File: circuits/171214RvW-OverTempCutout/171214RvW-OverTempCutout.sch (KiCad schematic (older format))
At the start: 6 parts

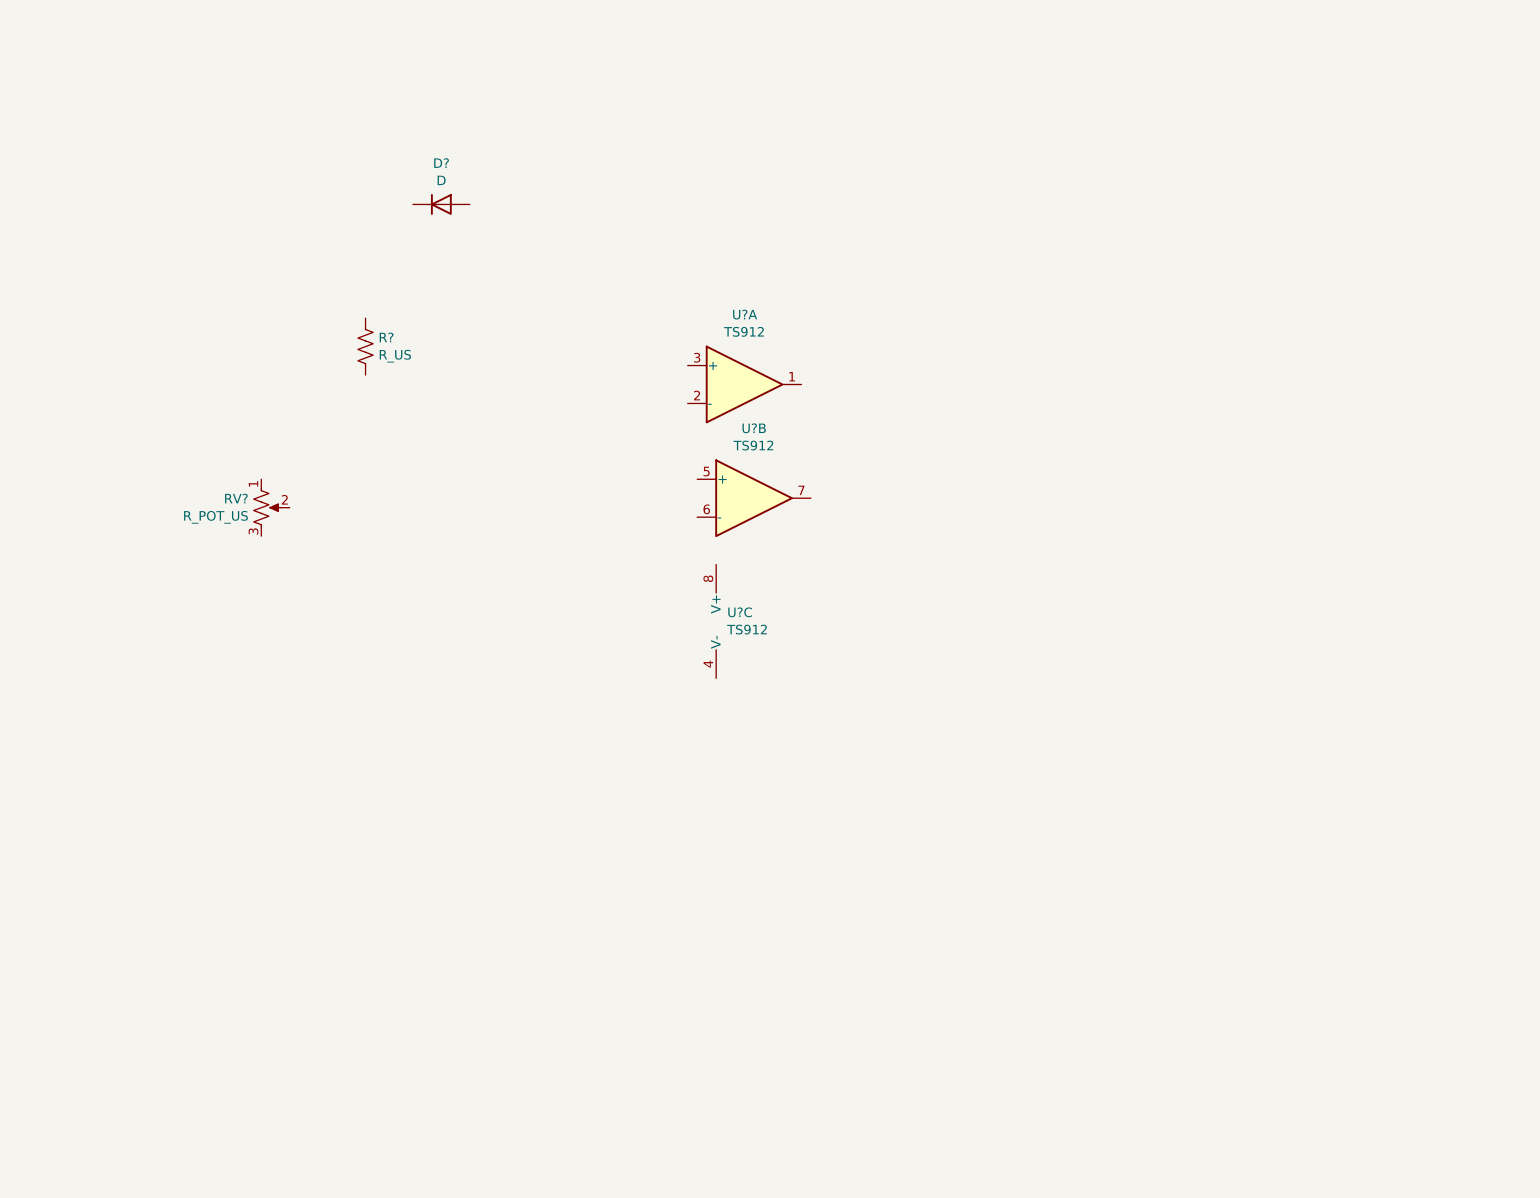
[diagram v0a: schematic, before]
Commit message: Overtemp Cutout done
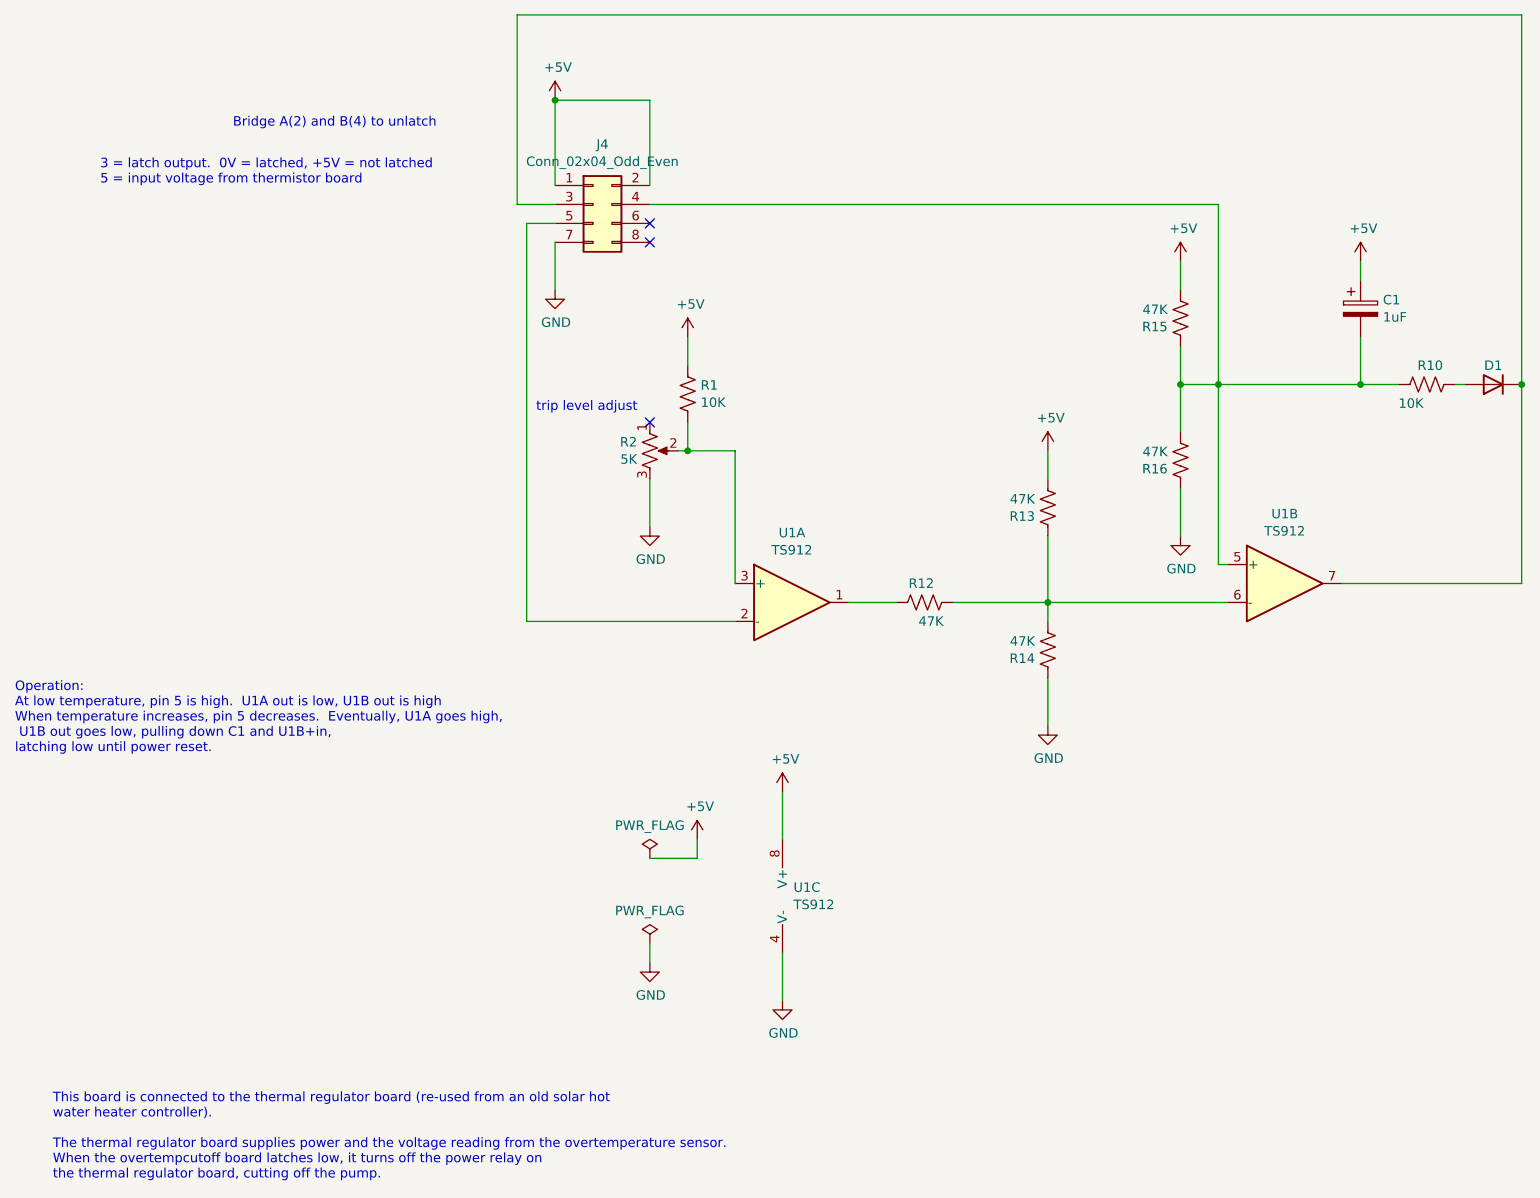
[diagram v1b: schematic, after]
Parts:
- added C1: 1uF, Capacitor_THT:C_Axial_L22.0mm_D9.5mm_P27.50mm_Horizontal, symbol Device:CP
- added J4: Conn_02x04_Odd_Even, Connector_PinHeader_2.54mm:PinHeader_2x04_P2.54mm_Vertical, symbol Connector_Generic:Conn_02x04_Odd_Even
- added R10: 10K, Resistor_THT:R_Axial_DIN0516_L15.5mm_D5.0mm_P20.32mm_Horizontal, symbol Device:R_US
- added R12, R13, R14, R15, R16: 47K, Resistor_THT:R_Axial_DIN0516_L15.5mm_D5.0mm_P20.32mm_Horizontal, symbol Device:R_US
- D1: renamed from D?; value D -> (none); footprint (none) -> Diode_THT:D_5KP_P10.16mm_Horizontal
- R1: renamed from R?; value R_US -> 10K; footprint (none) -> Resistor_THT:R_Axial_DIN0516_L15.5mm_D5.0mm_P20.32mm_Horizontal
- R2: renamed from RV?; value R_POT_US -> 5K; footprint (none) -> Potentiometer_THT:Potentiometer_Vishay_T73XX_Horizontal
- U1: renamed from U?; footprint (none) -> Package_DIP:DIP-8_W7.62mm
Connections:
- net at U1.1: now also R12.1
- net at U1.2 (-): now also J4.5 (Pin_5)
- net at U1.3 (+): now also R1.2, R2.2
- net at U1.5 (+): now also C1.2, J4.4 (Pin_4), R10.2, R15.1, R16.2
- net at U1.6 (-): now also R12.2, R13.1, R14.2
- net at U1.7: now also D1.1 (K), J4.3 (Pin_3)
- net GND: now reaches U1.4 (V-)
- net GND: now also R2.3, J4.7 (Pin_7), R14.1, R16.1
- net +5V: now reaches U1.8 (V+)
- net +5V: now also R1.1, C1.1, J4.1 (Pin_1), J4.2 (Pin_2), R13.2, R15.2
- net at D1.2 (A): now also R10.1
- no-connect marks 0 -> 3
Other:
- note added: "3 = latch output. 0V = latched, +5V = not latched\n5 = input voltage from thermistor board"
- note added: "Bridge A(2) and B(4) to unlatch"
- note added: "Operation:\nAt low temperature, pin 5 is high. U1A out is low, U1B out is high\nWhen temperature increases, pin 5 decreases. Eventually, U1A goes high,\n U1B out goes low, pulling down C1 and U1B+in, \nlatching low until power reset."
- note added: "This board is connected to the thermal regulator board (re-used from an old solar hot \nwater heater controller).\n\nThe thermal regulator board supplies power and the voltage reading from the overtemperature sensor.\nWhen the overtempcutoff board latches low, it turns off the power relay on \nthe thermal regulator board, cutting off the pump.\n"
- note added: "trip level adjust\n"
- moved on the sheet: D1, R1, R2, U1A, U1B, U1C
